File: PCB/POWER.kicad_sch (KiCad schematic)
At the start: 13 parts, among them J1 2604-3102, Q100 CSD19537Q3, Q101 BSS138, U100 TPS26631RGE

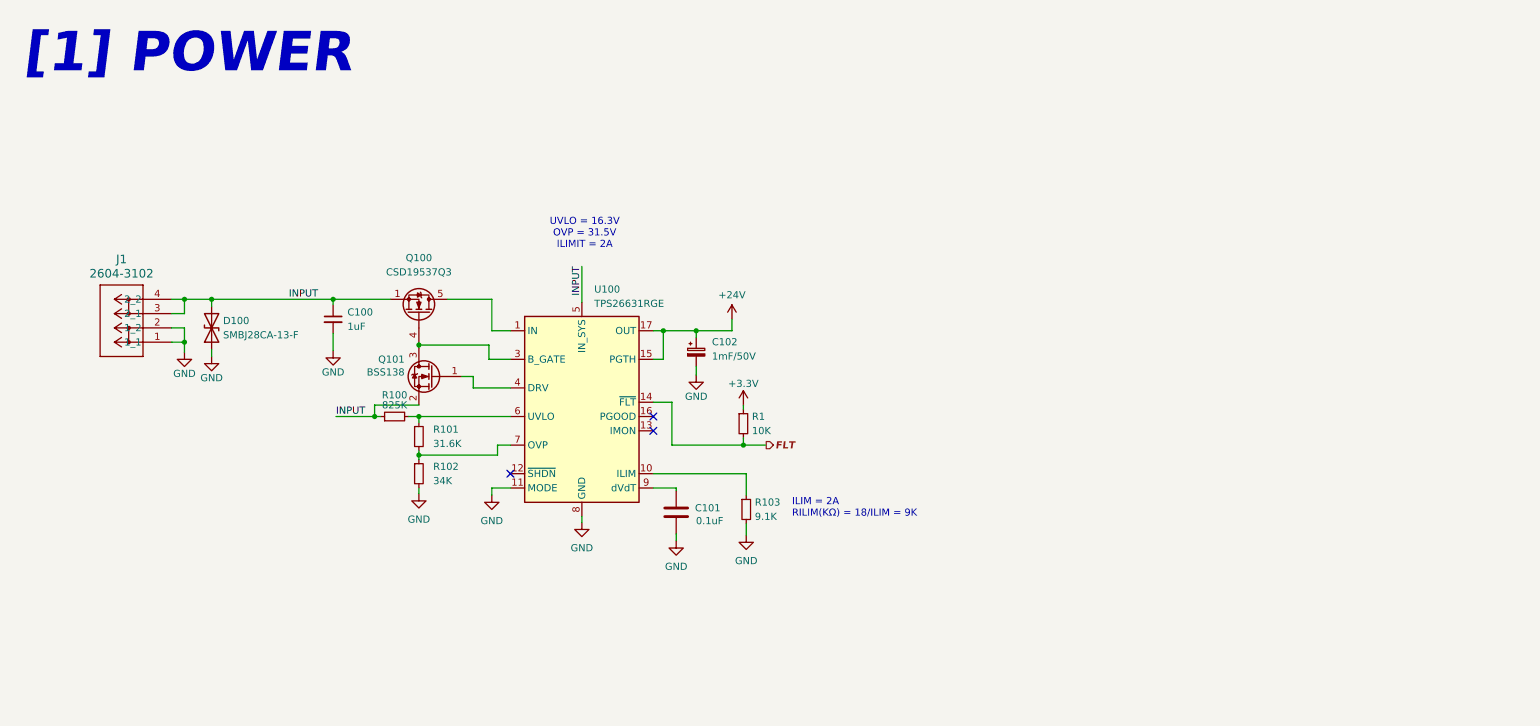
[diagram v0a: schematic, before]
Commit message: Diseño DC-DC
Se diseño las 2 etapas DC-DC:
- 24V a 12V con filtros
- 12V a 3.3V
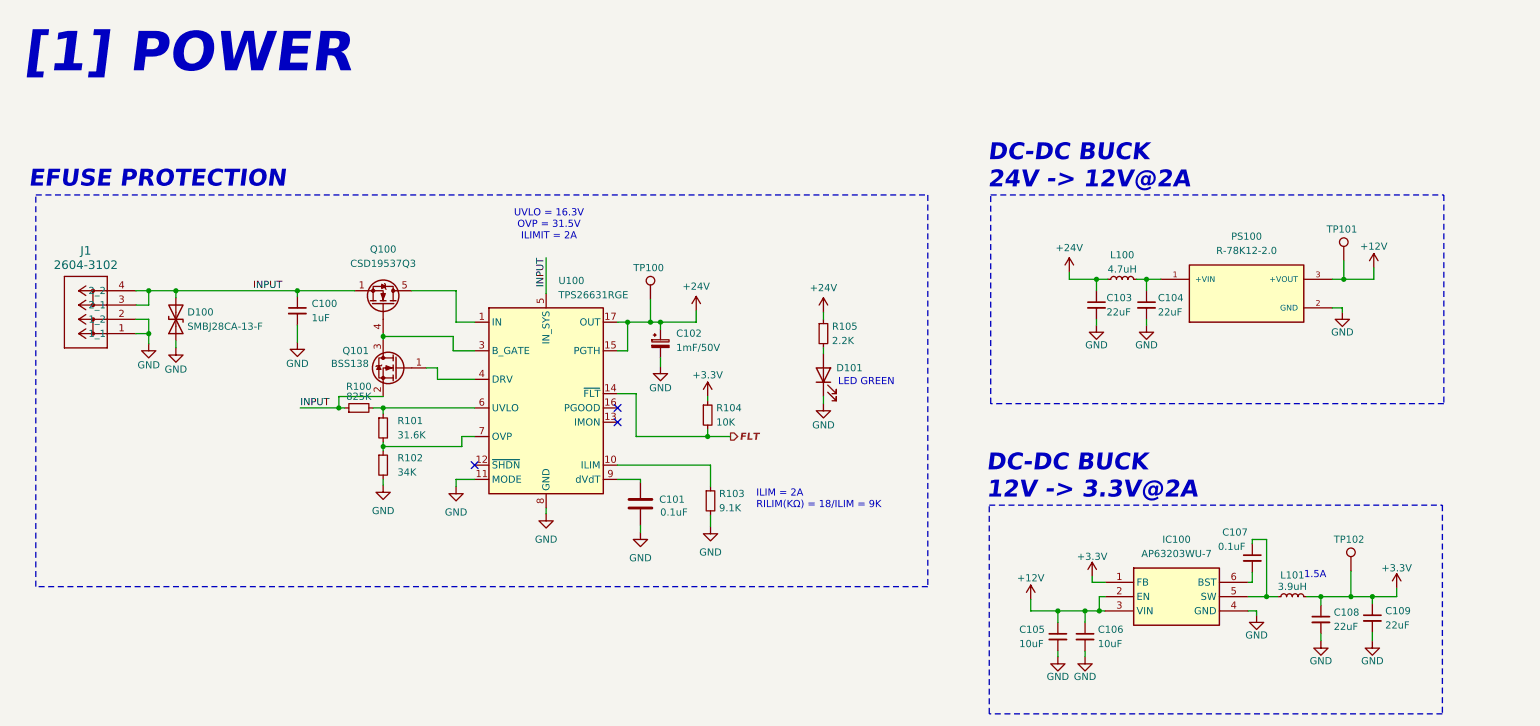
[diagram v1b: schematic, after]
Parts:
- added C103, C104: 22uF, Capacitor_SMD:C_1206_3216Metric, symbol Device:C_Small
- added C105, C106: 10uF, Capacitor_SMD:C_0805_2012Metric_Pad1.18x1.45mm_HandSolder, symbol Device:C_Small
- added C107: 0.1uF, Capacitor_SMD:C_0603_1608Metric_Pad1.08x0.95mm_HandSolder, symbol Device:C_Small
- added C108, C109: 22uF, Capacitor_SMD:C_0603_1608Metric_Pad1.08x0.95mm_HandSolder, symbol Device:C_Small
- added D101: 19-21/GHC-YR1S2/4T, LED_SMD:LED_0603_1608Metric, symbol Device:LED
- added IC100: AP63203WU-7, AP63203WU-7:AP63203WU7, symbol AP63203WU-7:AP63203WU-7
- added L100: 4.7uH, symbol Device:L_Small
- added L101: 3.9uH, Inductor_SMD:L_Sunlord_SWPA4030S, symbol Device:L_Small
- added PS100: R-78K12-2.0, R-78K12-2_0:R-78K12-2_0, symbol R-78K12-2_0:R-78K12-2.0
- added R105: 2.2K, Resistor_SMD:R_0603_1608Metric, symbol Device:R_Small
- added TP100, TP101, TP102: TestPoint, TestPoint:TestPoint_Pad_D2.0mm, symbol Connector:TestPoint
- renumbered R1 to R104
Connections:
- net +24V: now also C103.1, L100.1, R105.1, TP100.1
- net +3.3V: now also C108.1, C109.1, IC100.1 (FB), L101.2, TP102.1
- net GND: now also C103.2, C104.2, C105.2, C106.2, C108.2, C109.2, D101.1 (K), IC100.4 (GND), PS100.2 (GND)
- new net: C107.1, IC100.5 (SW), L101.1
- new net: C107.2, IC100.6 (BST)
- new net: D101.2 (A), R105.2
- new net: C104.1, L100.2, PS100.1 (+VIN)
- new net +12V: C105.1, C106.1, IC100.2 (EN), IC100.3 (VIN), PS100.3 (+VOUT), TP101.1
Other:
- note added: "1.5A"
- note added: "DC-DC BUCK 12V -> 3.3V@2A"
- note added: "DC-DC BUCK 24V -> 12V@2A"
- note added: "EFUSE PROTECTION"
- note added: "LED GREEN"
- moved on the sheet: C100, C101, C102, D100, J1, Q100, Q101, R100, R101, R102, R103, R104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

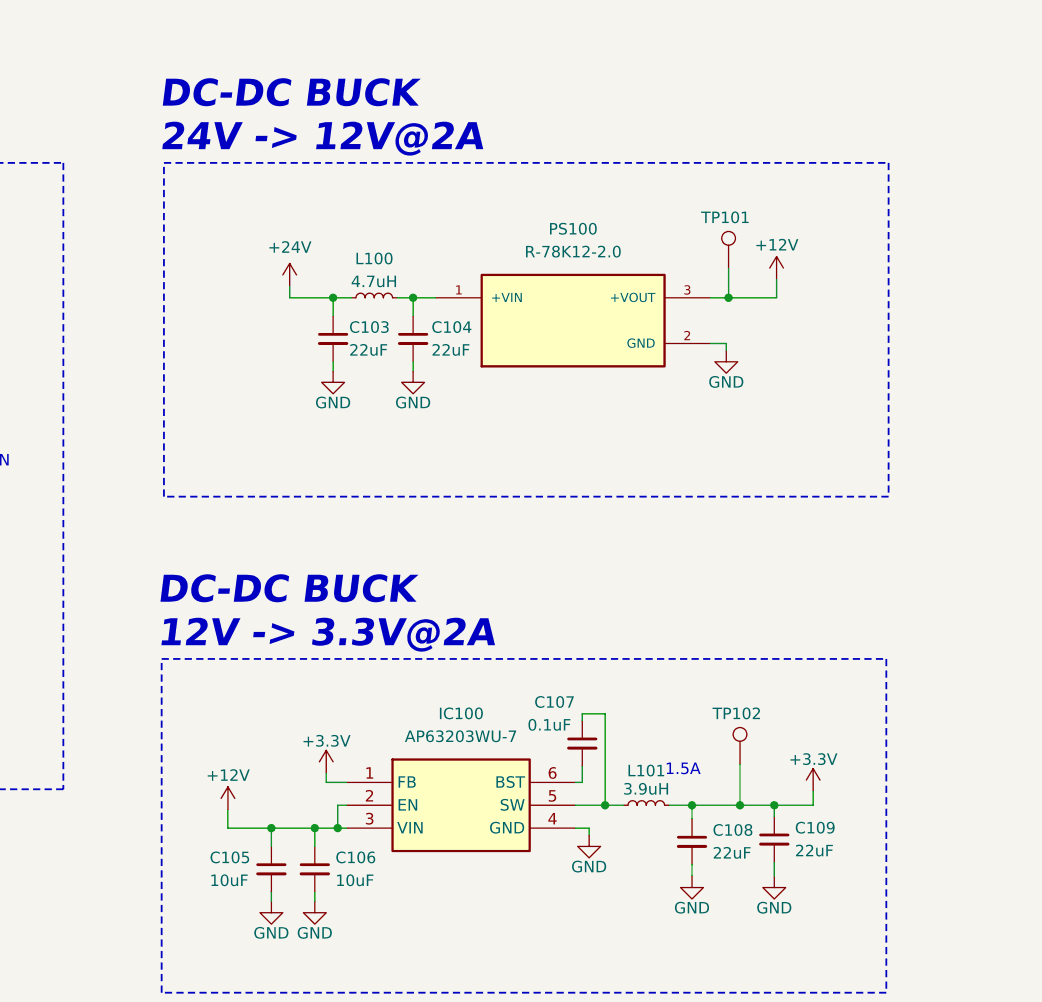
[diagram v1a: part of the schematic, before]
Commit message: Agregado RS485, Smart Switch, ORING Diode
Se termino de acabar todo el esquematico, solo falta crear el footprint para un inductor
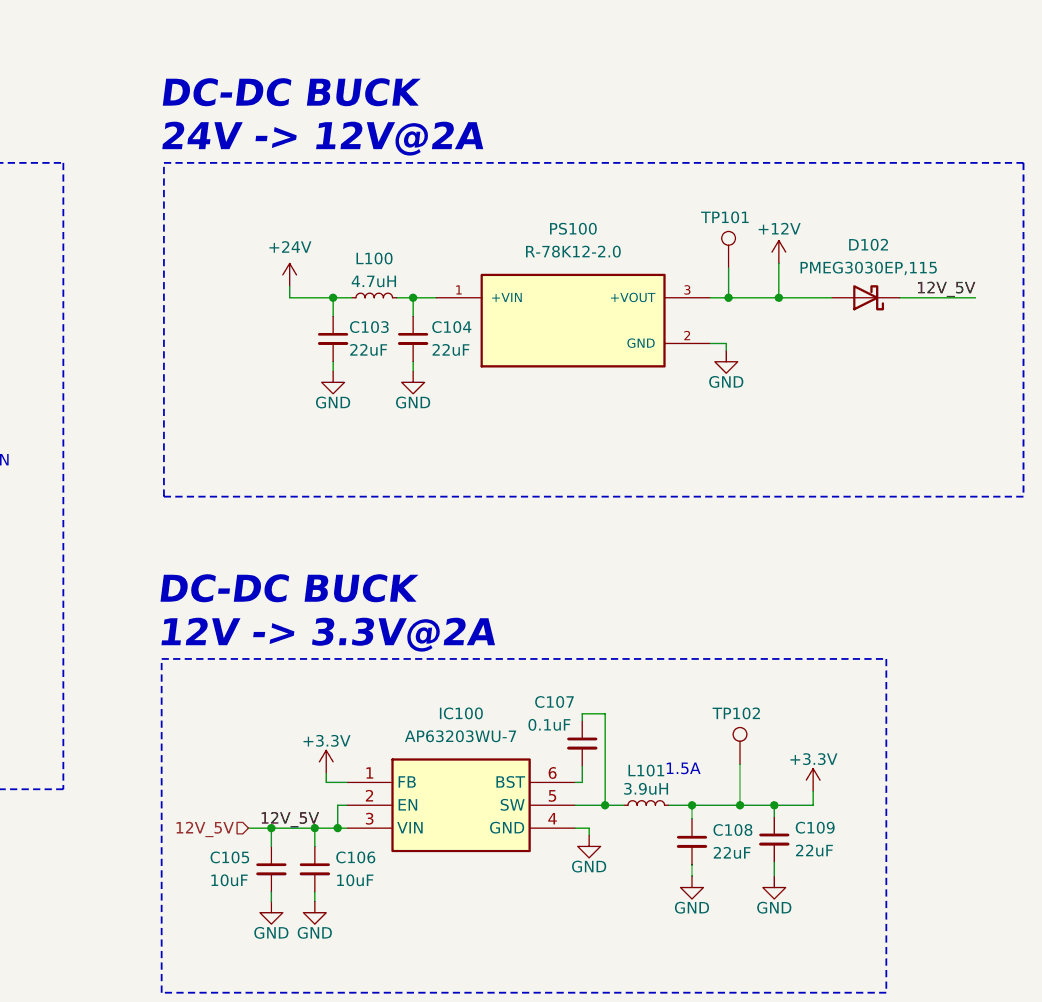
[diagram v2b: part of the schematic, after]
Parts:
- added D102: PMEG3030EP,115, Diode_SMD:D_SOD-128, symbol Diode:PMEG4050EP
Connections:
- net +12V: now also D102.2 (A); no longer C105.1, C106.1, IC100.2 (EN), IC100.3 (VIN)
- new net 12V_5V: C105.1, C106.1, D102.1 (K), IC100.2 (EN), IC100.3 (VIN)
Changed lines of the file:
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@@
 	)
 	(junction
+		(at 255.778 61.722)
+		(diameter 0)
+		(color 0 0 0 0)
+	)
+	(junction
 		(at 79.502 84.582)
 		(diameter 0)
@@
 	(wire
 		(pts
-			(xy 250.19 61.722) (xy 255.524 61.722)
+			(xy 250.19 61.722) (xy 255.778 61.722)
 		)
 		(stroke
@@
 	(wire
 		(pts
-			(xy 194.564 118.618) (xy 194.564 120.65)
-		)
-		(stroke
-			(width 0)
-			(type default)
-		)
-	)
-	(wire
-		(pts
-			(xy 255.524 59.69) (xy 255.524 61.722)
+			(xy 255.778 57.912) (xy 255.778 61.722)
 		)
 		(stroke
@@
 	(wire
 		(pts
-			(xy 194.564 120.65) (xy 199.39 120.65)
+			(xy 196.85 120.65) (xy 199.39 120.65)
 		)
 		(stroke
@@
 	(wire
 		(pts
+			(xy 269.24 61.722) (xy 277.622 61.722)
+		)
+		(stroke
+			(width 0)
+			(type default)
+		)
+	)
+	(wire
+		(pts
 			(xy 35.56 68.834) (xy 37.846 68.834)
 		)
@@
 	(wire
 		(pts
+			(xy 255.778 61.722) (xy 261.62 61.722)
+		)
+		(stroke
+			(width 0)
+			(type default)
+		)
+	)
+	(wire
+		(pts
 			(xy 92.456 97.282) (xy 92.456 98.552)
 		)
@@
 	(rectangle
 		(start 187.452 46.736)
-		(end 267.97 83.82)
+		(end 282.956 83.82)
 		(stroke
 			(width 0.2)
@@
 		)
 	)
+	(label "12V_5V"
+		(at 198.12 120.65 0)
+		(fields_autoplaced yes)
+		(effects
+			(font
+				(size 1.27 1.27)
+			)
+			(justify left bottom)
+		)
+	)
+	(label "12V_5V"
+		(at 277.622 61.722 180)
+		(fields_autoplaced yes)
+		(effects
+			(font
+				(size 1.27 1.27)
+			)
+			(justify right bottom)
+		)
+	)
 	(label "INPUT"
 		(at 56.388 63.754 0)
@@
 		)
 	)
+	(hierarchical_label "12V_5V"
+		(shape input)
+		(at 196.85 120.65 180)
+		(fields_autoplaced yes)
+		(effects
+			(font
+				(size 1.27 1.27)
+			)
+			(justify right)
+		)
+	)
 	(symbol
 		(lib_id "Device:C_Small")
@@
 	)
 	(symbol
+		(lib_id "Diode:PMEG4050EP")
+		(at 265.43 61.722 180)
+		(unit 1)
+		(exclude_from_sim no)
+		(in_bom yes)
+		(on_board yes)
+		(dnp no)
+		(fields_autoplaced yes)
+		(property "Reference" "D102"
+			(at 265.7475 55.88 0)
+			(effects
+				(font
+					(size 1.27 1.27)
+				)
+			)
+		)
+		(property "Value" "PMEG3030EP,115"
+			(at 265.7475 58.42 0)
+			(effects
+				(font
+					(size 1.27 1.27)
+				)
+			)
+		)
+		(property "Footprint" "Diode_SMD:D_SOD-128"
+			(at 265.43 57.277 0)
+			(effects
+				(font
+					(size 1.27 1.27)
+				)
+				(hide yes)
+			)
+		)
+		(property "Datasheet" "https://assets.nexperia.com/documents/data-sheet/PMEG4050EP.pdf"
+			(at 265.43 61.722 0)
+			(effects
+				(font
+					(size 1.27 1.27)
+				)
+				(hide yes)
+			)
+		)
+		(property "Description" "40V, 5A low Vf Schottky barrier rectifier, SOD-128"
+			(at 265.43 61.722 0)
+			(effects
+				(font
+					(size 1.27 1.27)
+				)
+				(hide yes)
+			)
+		)
+		(property "LCSC" "C255587"
+			(at 265.43 61.722 0)
+			(effects
+				(font
+					(size 1.27 1.27)
+				)
+				(hide yes)
+			)
+		)
+		(pin "2"
+		)
+		(pin "1"
+		)
+		(instances
+			(project ""
+				(path "/118ffa26-3c65-424a-af71-04338c4de0b0/e2751aaa-40ab-491e-8724-b4cb7cd2712b"
+					(reference "D102")
+					(unit 1)
+				)
+			)
+		)
+	)
+	(symbol
 		(lib_id "Device:R_Small")
 		(at 75.184 84.582 90)
@@
 	(symbol
 		(lib_id "power:+12V")
-		(at 255.524 59.69 0)
+		(at 255.778 57.912 0)
 		(unit 1)
 		(exclude_from_sim no)
@@
 		(dnp no)
 		(property "Reference" "#PWR023"
-			(at 255.524 63.5 0)
+			(at 255.778 61.722 0)
 			(effects
 				(font
@@
 		)
 		(property "Value" "+12V"
-			(at 255.524 55.88 0)
+			(at 255.778 54.102 0)
 			(effects
 				(font
@@
 		)
 		(property "Footprint" ""
-			(at 255.524 59.69 0)
+			(at 255.778 57.912 0)
 			(effects
 				(font
@@
 		)
 		(property "Datasheet" ""
-			(at 255.524 59.69 0)
+			(at 255.778 57.912 0)
 			(effects
 				(font
@@
 		)
 		(property "Description" "Power symbol creates a global label with name \"+12V\""
-			(at 255.524 59.69 0)
+			(at 255.778 57.912 0)
 			(effects
 				(font
@@
 					(unit 1)
 				)
-			)
-		)
-	)
-	(symbol
-		(lib_id "power:+12V")
-		(at 194.564 118.618 0)
-		(unit 1)
-		(exclude_from_sim no)
-		(in_bom yes)
-		(on_board yes)
-		(dnp no)
-		(property "Reference" "#PWR021"
-			(at 194.564 122.428 0)
-			(effects
-				(font
-					(size 1.27 1.27)
-				)
-				(hide yes)
-			)
-		)
-		(property "Value" "+12V"
-			(at 194.564 114.808 0)
-			(effects
-				(font
-					(size 1.27 1.27)
-				)
-			)
-		)
-		(property "Footprint" ""
-			(at 194.564 118.618 0)
-			(effects
-				(font
-					(size 1.27 1.27)
-				)
-				(hide yes)
-			)
-		)
-		(property "Datasheet" ""
-			(at 194.564 118.618 0)
-			(effects
-				(font
-					(size 1.27 1.27)
-				)
-				(hide yes)
-			)
-		)
-		(property "Description" "Power symbol creates a global label with name \"+12V\""
-			(at 194.564 118.618 0)
-			(effects
-				(font
-					(size 1.27 1.27)
-				)
-				(hide yes)
-			)
-		)
-		(pin "1"
-		)
-		(instances
-			(project "PCB-Cuarto"
-				(path "/118ffa26-3c65-424a-af71-04338c4de0b0/e2751aaa-40ab-491e-8724-b4cb7cd2712b"
-					(reference "#PWR021")
-					(unit 1)
-				)

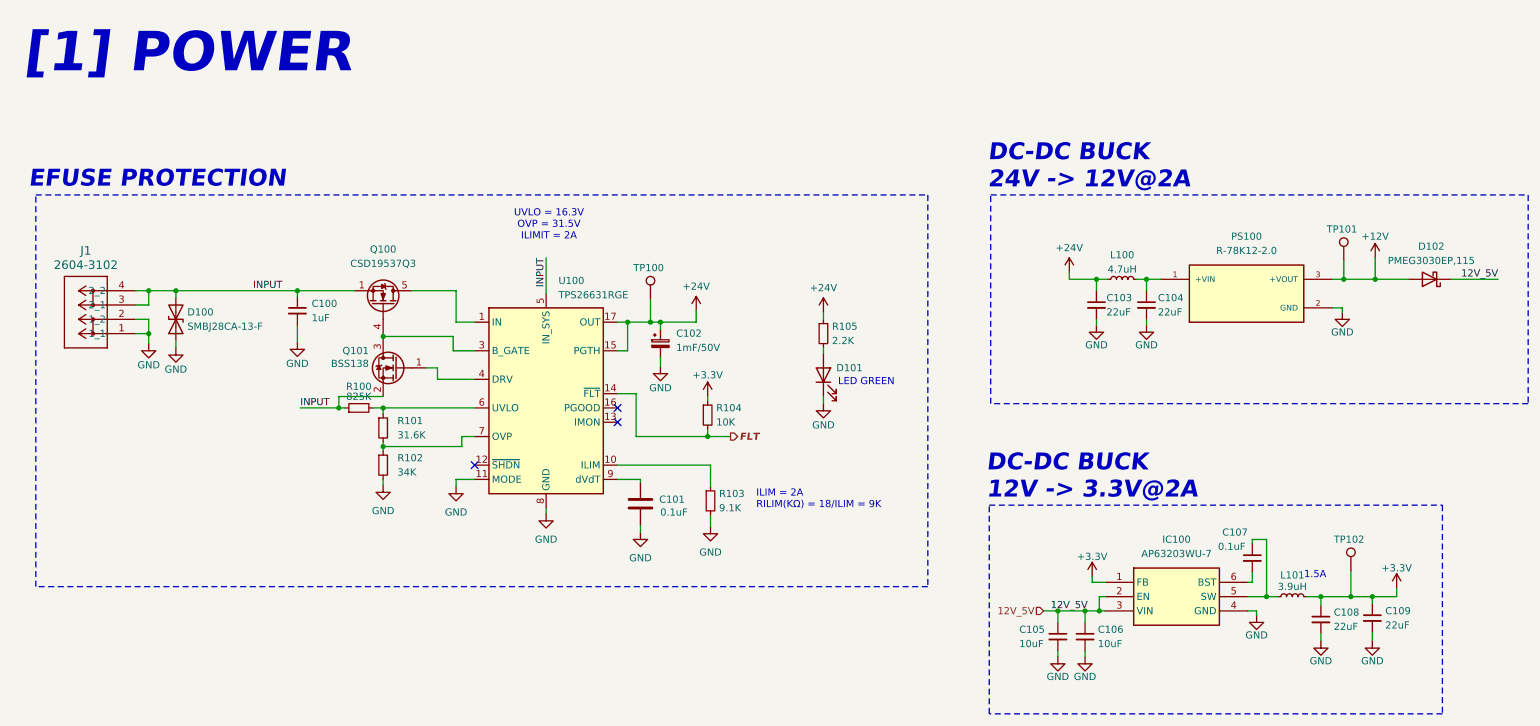
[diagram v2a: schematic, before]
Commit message: Placement
Se termino de crear el footprint para el inductor y placement en la PCB
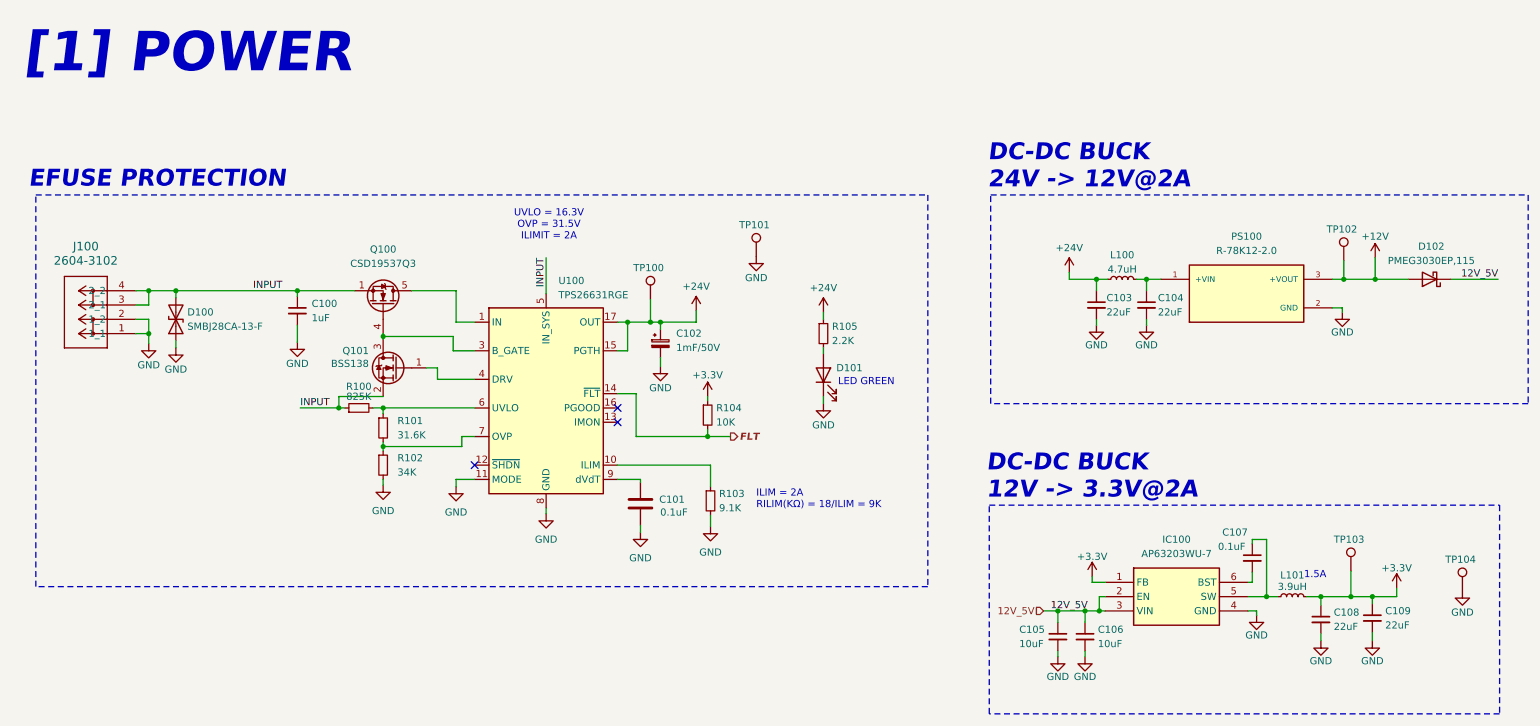
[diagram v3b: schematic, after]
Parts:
- added TP101, TP104: TestPoint, TestPoint:TestPoint_Pad_D2.0mm, symbol Connector:TestPoint
- C101: footprint Capacitor_SMD:C_0402_1005Metric -> Capacitor_SMD:C_0603_1608Metric; LCSC C1525 -> C14663
- L100: footprint (none) -> MDA5030-4R7M:MDA5030-4R7M
- renumbered J1 to J100, TP101 to TP102, TP102 to TP103
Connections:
- net GND: now also TP101.1, TP104.1
